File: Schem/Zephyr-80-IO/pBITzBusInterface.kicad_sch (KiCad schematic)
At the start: 1 part, among them J1 pBITzBus

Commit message: Added all the manufacturer part numbers to the KiCad schematics and PCB files. This will make it easier to order the parts for the project and ensure that the correct components are used. I also removed some of the old schematics that were no longer needed, such as the BaudClock, ConsolePort, DeviceSelectDecode, GPIOUserSerial, IO Controller, UserPorts, Video, and Z80HomeBrew schematics. These changes will help to streamline the design and make it easier to understand.
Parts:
- J1: now left out of the parts list
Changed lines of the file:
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@@
 		(unit 2)
 		(exclude_from_sim no)
-		(in_bom yes)
+		(in_bom no)
 		(on_board yes)
 		(dnp no)
@@
 		(unit 3)
 		(exclude_from_sim no)
-		(in_bom yes)
+		(in_bom no)
 		(on_board yes)
 		(dnp no)
@@
 		(unit 1)
 		(exclude_from_sim no)
-		(in_bom yes)
+		(in_bom no)
 		(on_board yes)
 		(dnp no)

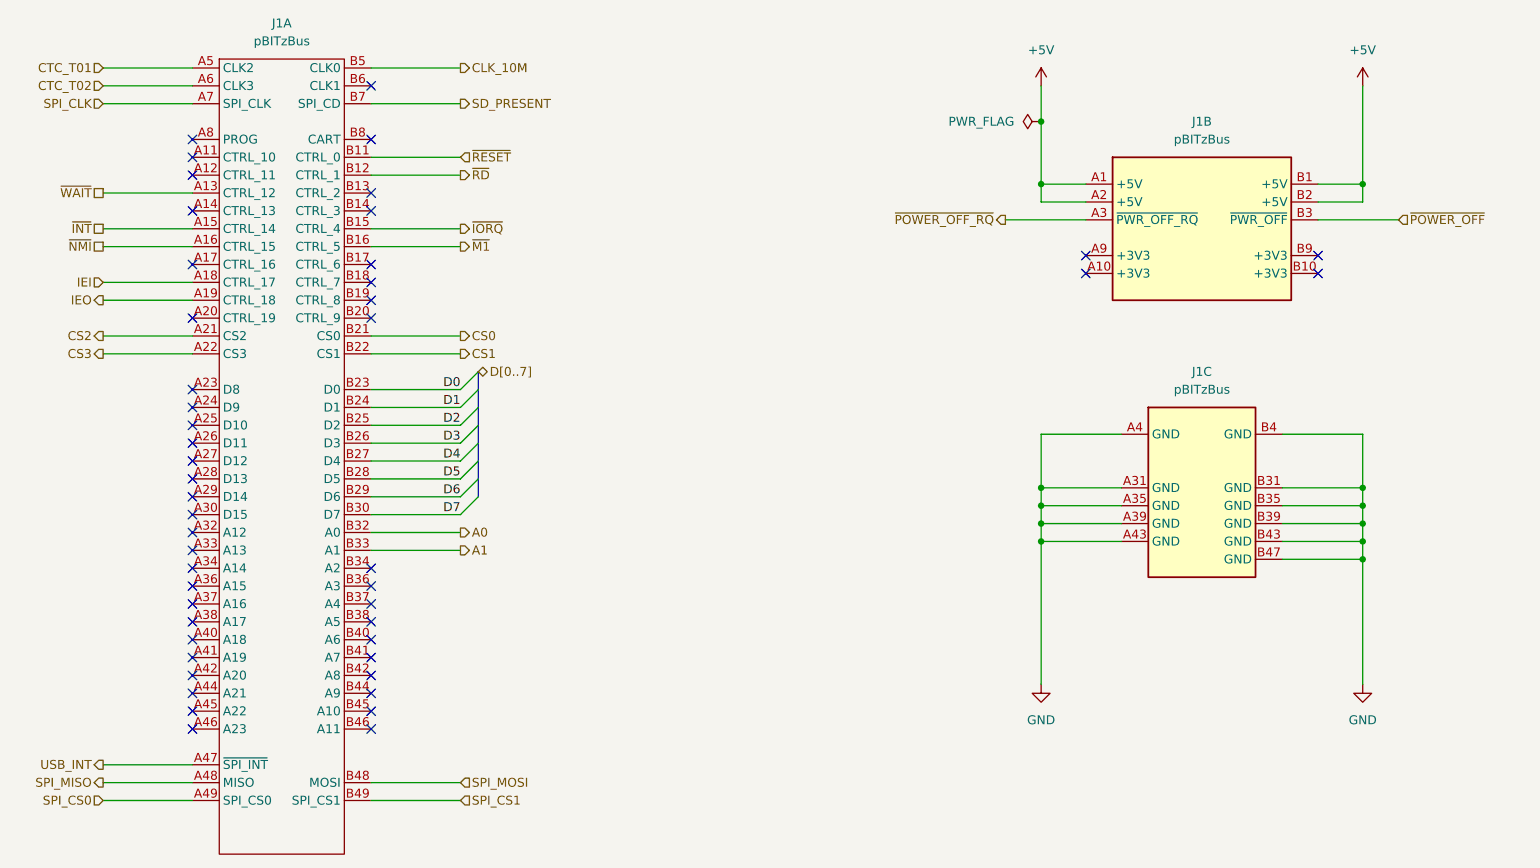
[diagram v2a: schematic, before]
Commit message: Updated the IO Controller to properly support SDLC and SPI.
* Separated SPI1 and SPI2 and associated to the right pins.
      SPI1 is for devices (USB, SD Card and Controllers)
      SPI2 is for the SDLC controller (Z80 SIO1/A and B)

* Fixed the 1.27mm vs 2.54mm pin headers
* Fixed the power sequencing
* Fixed the pull ups
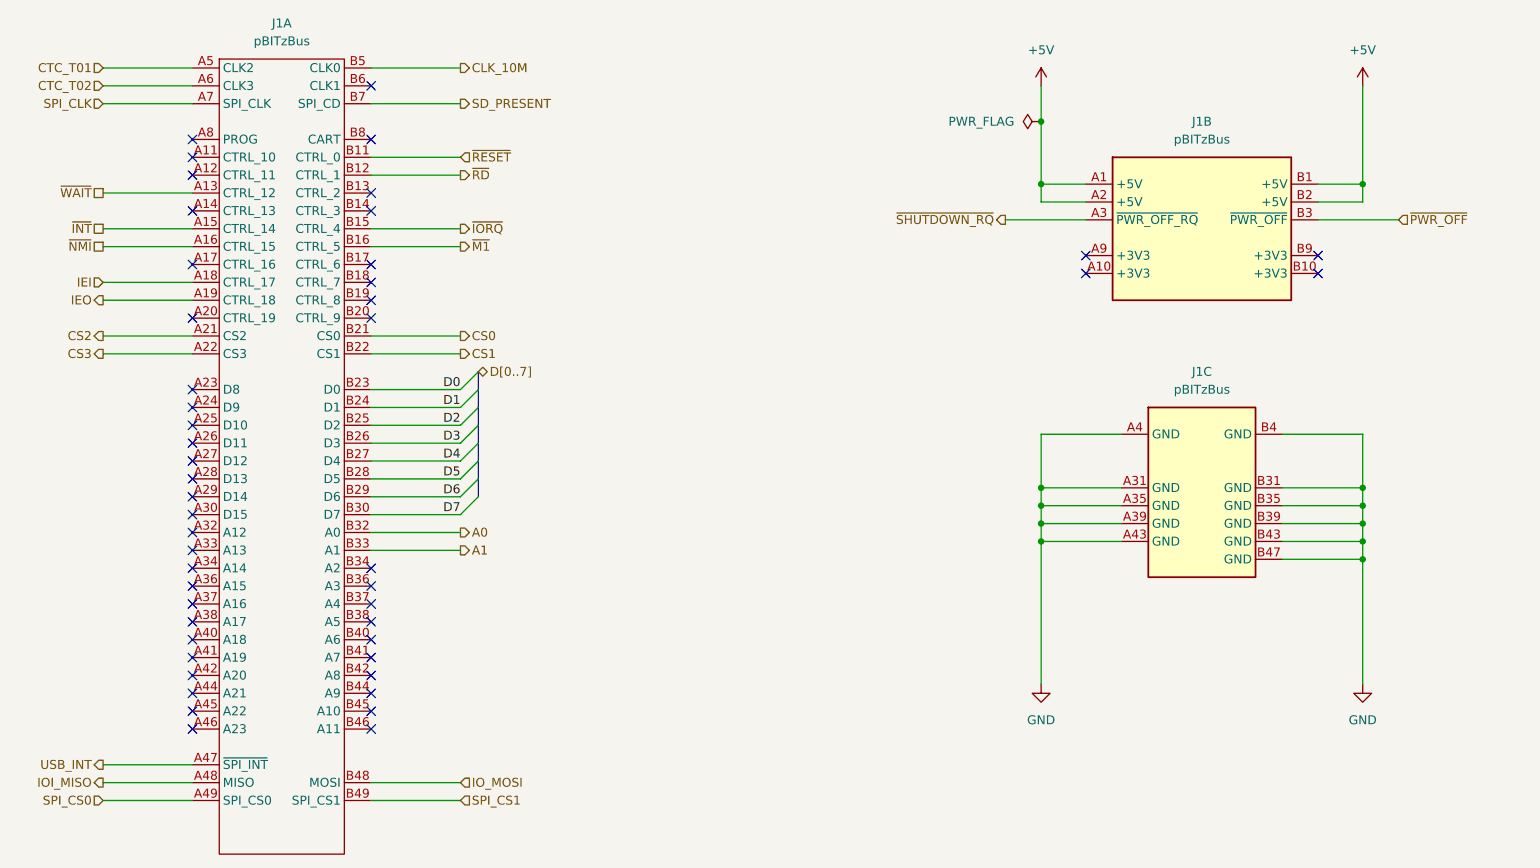
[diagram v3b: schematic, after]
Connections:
- net SPI_MISO renamed IOI_MISO
- net SPI_MOSI renamed IO_MOSI
- net ~{POWER_OFF_RQ} renamed ~{SHUTDOWN_RQ}
- net ~{POWER_OFF} renamed ~{PWR_OFF}
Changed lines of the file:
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@@
 		)
 	)
-	(hierarchical_label "~{POWER_OFF_RQ}"
+	(hierarchical_label "~{SHUTDOWN_RQ}"
 		(shape output)
 		(at 223.52 147.32 180)
@@
 		)
 	)
-	(hierarchical_label "SPI_MISO"
+	(hierarchical_label "IOI_MISO"
 		(shape output)
 		(at 95.25 227.33 180)
@@
 		)
 	)
-	(hierarchical_label "~{POWER_OFF}"
+	(hierarchical_label "~{PWR_OFF}"
 		(shape input)
 		(at 279.4 147.32 0)
@@
 		)
 	)
-	(hierarchical_label "SPI_MOSI"
+	(hierarchical_label "IO_MOSI"
 		(shape input)
 		(at 146.05 227.33 0)
